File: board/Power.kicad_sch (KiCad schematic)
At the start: 0 parts

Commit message: Added MCU and initial half bridge circuits from application circuit.
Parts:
- added C6: 10µF, Capacitor_SMD:C_1206_3216Metric_Pad1.33x1.80mm_HandSolder, symbol Device:C
- added C7: 10µF, Capacitor_SMD:C_0603_1608Metric_Pad1.08x0.95mm_HandSolder, symbol Device:C
- added Conn1: AndersonPP, symbol MRDT_Connectors:AndersonPP
- added D1, D2, D3: Green, symbol Device:LED
- added R14, R5: 220 Ω, symbol Device:R
- added R4: 1.5 kΩ, symbol Device:R
- added U3: OKI, MRDT_Devices:OKI_Horizontal, symbol MRDT_Devices:OKI
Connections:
- new net: D1.2 (A), R4.2
- new net: D2.2 (A), R5.2
- new net: D3.2 (A), R14.2
- new net +3.3V: R14.1
- new net +5V: C7.1, R5.1, U3.3 (Vo)
- new net GND: C6.2, C7.2, Conn1.1 (GND), D1.1 (K), D2.1 (K), D3.1 (K), U3.2 (GND)
- new net VCC: C6.1, Conn1.4 (PV+), R4.1, U3.1 (Vi)
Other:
- note added: "Power"
- note added: "Power LEDs"

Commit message: Added connections around the MCU from the application circuit from the data sheet, VCC, VDD, VREF+, etc.
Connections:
- net VCC renamed VM
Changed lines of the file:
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@@
 		(on_board yes)
 		(dnp no)
-		(fields_autoplaced yes)
 		(property "Reference" "#PWR019"
 			(at 43.18 30.48 0)
@@
 			)
 		)
-		(property "Value" "VCC"
-			(at 43.18 21.59 0)
-			(effects
-				(font
-					(size 1.27 1.27)
-				)
+		(property "Value" "VM"
+			(at 41.656 22.098 0)
+			(effects
+				(font
+					(size 1.27 1.27)
+				)
+				(justify left)
 			)
 		)
@@
 		(on_board yes)
 		(dnp no)
-		(fields_autoplaced yes)
 		(property "Reference" "#PWR017"
 			(at 31.75 29.21 0)
@@
 			)
 		)
-		(property "Value" "VCC"
-			(at 31.75 20.32 0)
-			(effects
-				(font
-					(size 1.27 1.27)
-				)
+		(property "Value" "VM"
+			(at 30.48 21.59 0)
+			(effects
+				(font
+					(size 1.27 1.27)
+				)
+				(justify left)
 			)
 		)
@@
 		(on_board yes)
 		(dnp no)
-		(fields_autoplaced yes)
 		(property "Reference" "#PWR07"
 			(at 78.74 29.21 0)
@@
 			)
 		)
-		(property "Value" "VCC"
-			(at 78.74 20.32 0)
-			(effects
-				(font
-					(size 1.27 1.27)
-				)
-			)
-		)
+		(property "Value" "VM"
+			(at 77.216 21.59 0)
+			(effects
+				(font
+					(size 1.27 1.27)
+				)
+				(justify left)
+			)
+		)

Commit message: Finished adding component values to circuits, except for 4 filtering capacitors
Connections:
- net +3.3V renamed VDD_2
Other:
- note added: "+3.3 V"
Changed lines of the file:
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@@
+		)
+	)
+	(text "+3.3 V"
+		(exclude_from_sim no)
+		(at 77.978 44.45 0)
+		(effects
+			(font
+				(size 1.27 1.27)
+			)
 		)
 	)
@@
 	(wire
 		(pts
-			(xy 78.74 44.45) (xy 78.74 46.99)
-		)
-		(stroke
-			(width 0)
-			(type default)
-		)
-	)
-	(wire
-		(pts
 			(xy 78.74 38.1) (xy 85.09 38.1)
 		)
@@
 	(wire
 		(pts
-			(xy 78.74 46.99) (xy 85.09 46.99)
+			(xy 82.55 46.99) (xy 85.09 46.99)
 		)
 		(stroke
@@
 			(width 0)
 			(type default)
+		)
+	)
+	(global_label "VDD_2"
+		(shape input)
+		(at 82.55 46.99 180)
+		(fields_autoplaced yes)
+		(effects
+			(font
+				(size 1.27 1.27)
+			)
+			(justify right)
+		)
+		(property "Intersheetrefs" "${INTERSHEET_REFS}"
+			(at 73.7591 46.99 0)
+			(effects
+				(font
+					(size 1.27 1.27)
+				)
+				(justify right)
+				(hide yes)
+			)
 		)
 	)
@@
 					(unit 1)
 				)
-			)
-		)
-	)
-	(symbol
-		(lib_id "power:+3.3V")
-		(at 78.74 44.45 0)
-		(unit 1)
-		(exclude_from_sim no)
-		(in_bom yes)
-		(on_board yes)
-		(dnp no)
-		(property "Reference" "#PWR025"
-			(at 78.74 48.26 0)
-			(effects
-				(font
-					(size 1.27 1.27)
-				)
-				(hide yes)
-			)
-		)
-		(property "Value" "+3.3V"
-			(at 78.74 40.386 0)
-			(effects
-				(font
-					(size 1.27 1.27)
-				)
-			)
-		)
-		(property "Footprint" ""
-			(at 78.74 44.45 0)
-			(effects
-				(font
-					(size 1.27 1.27)
-				)
-				(hide yes)
-			)
-		)
-		(property "Datasheet" ""
-			(at 78.74 44.45 0)
-			(effects
-				(font
-					(size 1.27 1.27)
-				)
-				(hide yes)
-			)
-		)
-		(property "Description" "Power symbol creates a global label with name \"+3.3V\""
-			(at 78.74 44.45 0)
-			(effects
-				(font
-					(size 1.27 1.27)
-				)
-				(hide yes)
-			)
-		)
-		(pin "1"
-		)
-		(instances
-			(project ""
-				(path "/1ef8bc88-f0df-4a97-862b-c4b9ec3b4ed0/b855338b-ea17-4b47-9bba-97d28962f939"
-					(reference "#PWR025")
-					(unit 1)
-				)

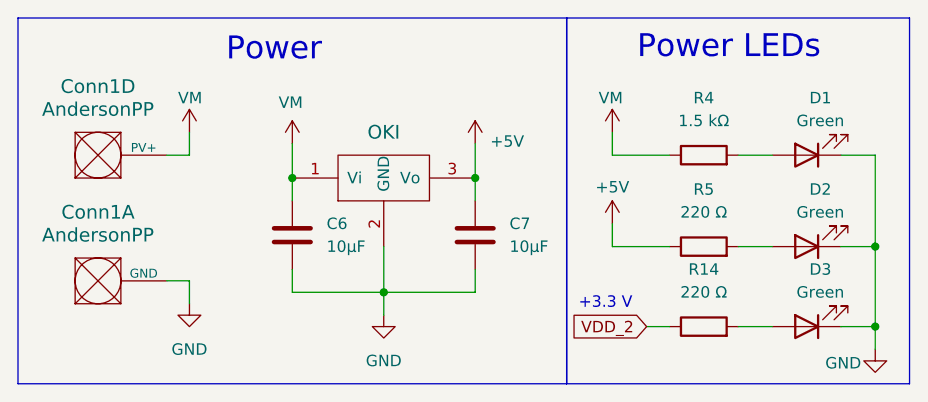
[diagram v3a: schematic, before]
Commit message: Implemented some fixes discussed during the board review.
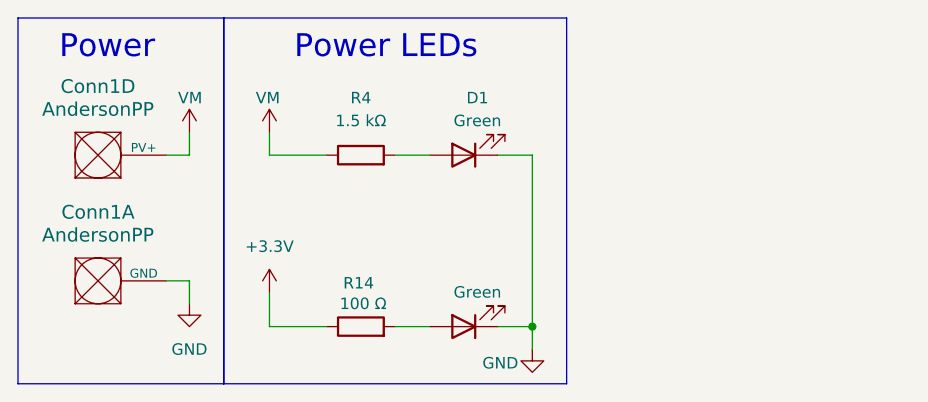
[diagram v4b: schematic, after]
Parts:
- removed C6: 10µF, Capacitor_SMD:C_1206_3216Metric_Pad1.33x1.80mm_HandSolder, symbol Device:C
- removed C7: 10µF, Capacitor_SMD:C_0603_1608Metric_Pad1.08x0.95mm_HandSolder, symbol Device:C
- removed D2: Green, symbol Device:LED
- removed R5: 220 Ω, symbol Device:R
- removed U3: OKI, MRDT_Devices:OKI_Horizontal, symbol MRDT_Devices:OKI
- R14: value 220 Ω -> 100 Ω
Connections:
- net VDD_2 renamed +3.3V
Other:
- note removed: "+3.3 V"
- moved on the sheet: D1, R14, R4

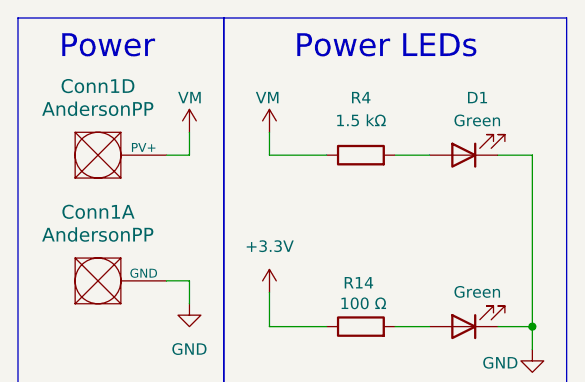
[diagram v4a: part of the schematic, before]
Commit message: Fixed many issues brought up in the schematic review.
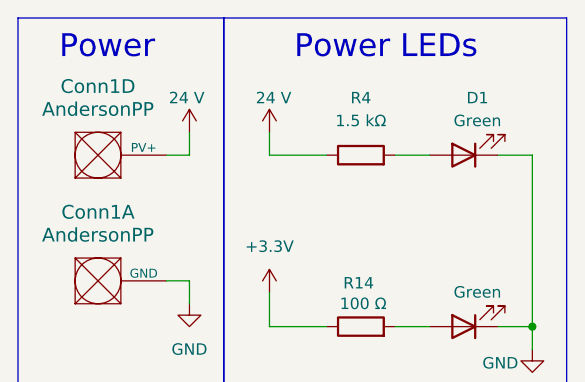
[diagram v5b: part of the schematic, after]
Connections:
- net VM renamed 24 V
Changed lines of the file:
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@@
 			)
 		)
-		(property "Value" "VM"
-			(at 30.48 21.59 0)
+		(property "Value" "24 V"
+			(at 29.464 21.59 0)
 			(effects
 				(font
@@
 			)
 		)
-		(property "Value" "VM"
+		(property "Value" "24 V"
 			(at 39.116 21.59 0)
 			(effects

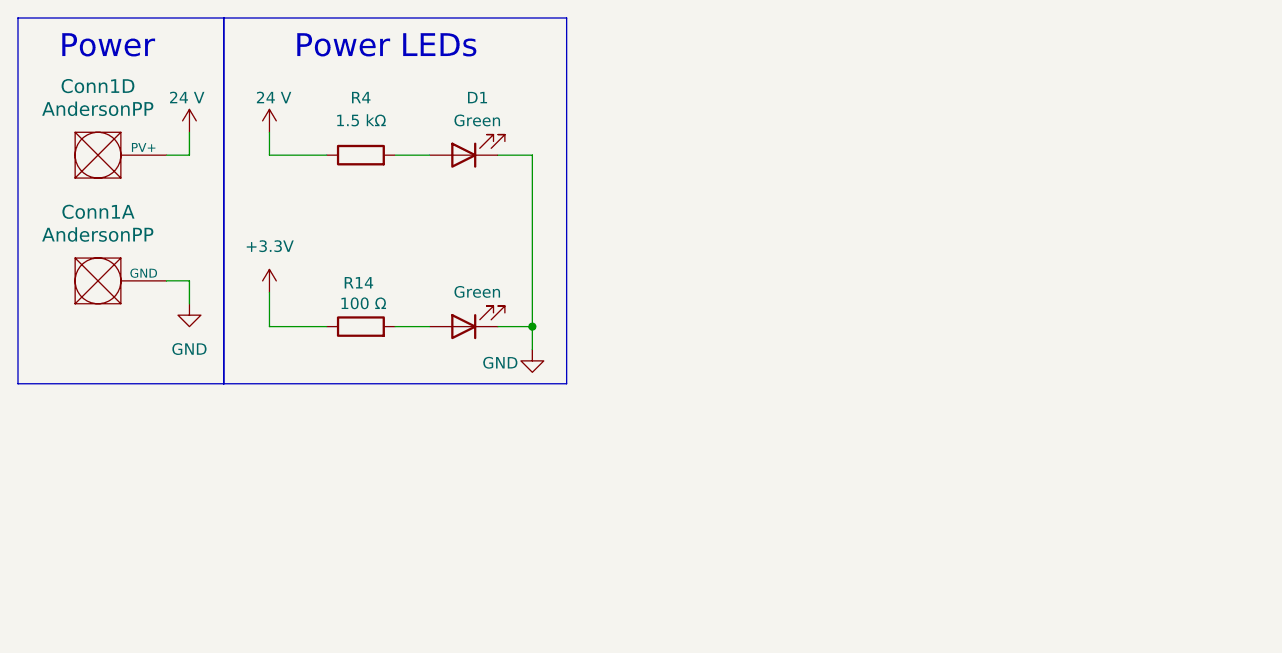
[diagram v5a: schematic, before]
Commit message: Fixed everything mentioned in schematic review, should be ready for second review/layout.
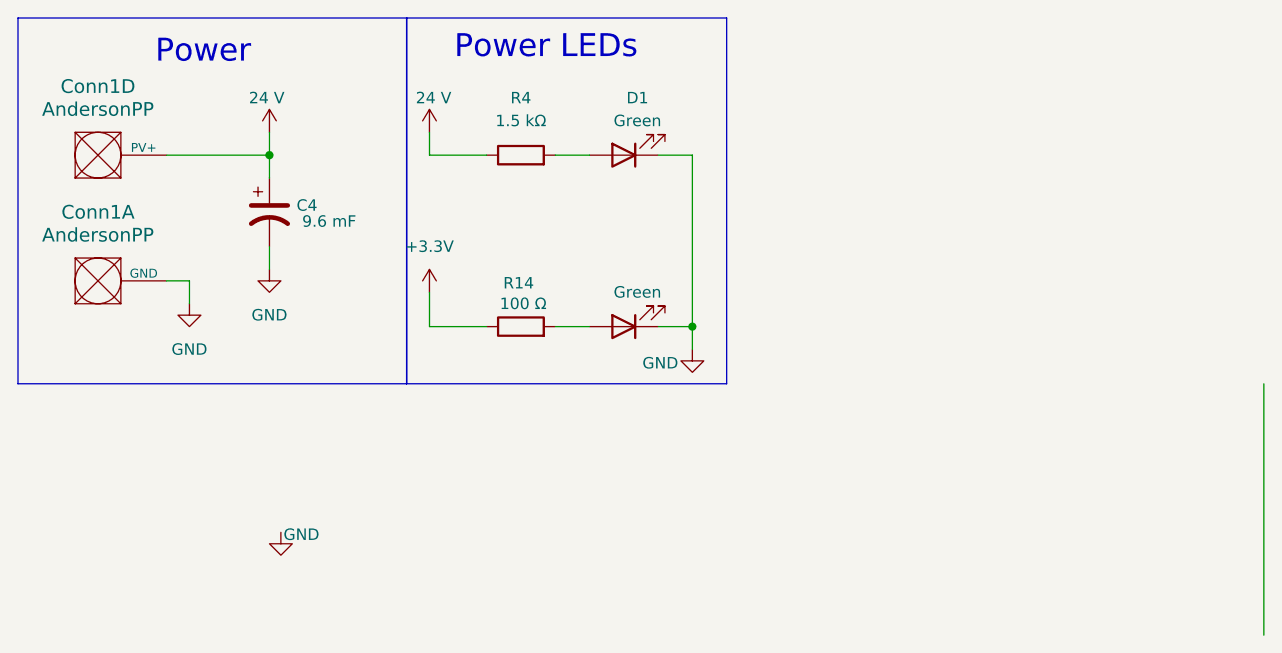
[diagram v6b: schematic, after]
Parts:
- added C4: 9.6 mF, symbol Device:C_Polarized_US
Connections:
- net 24 V: now also C4.1
- net GND: now also C4.2
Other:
- moved on the sheet: D1, R14, R4

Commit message: Updated footprints for schematic
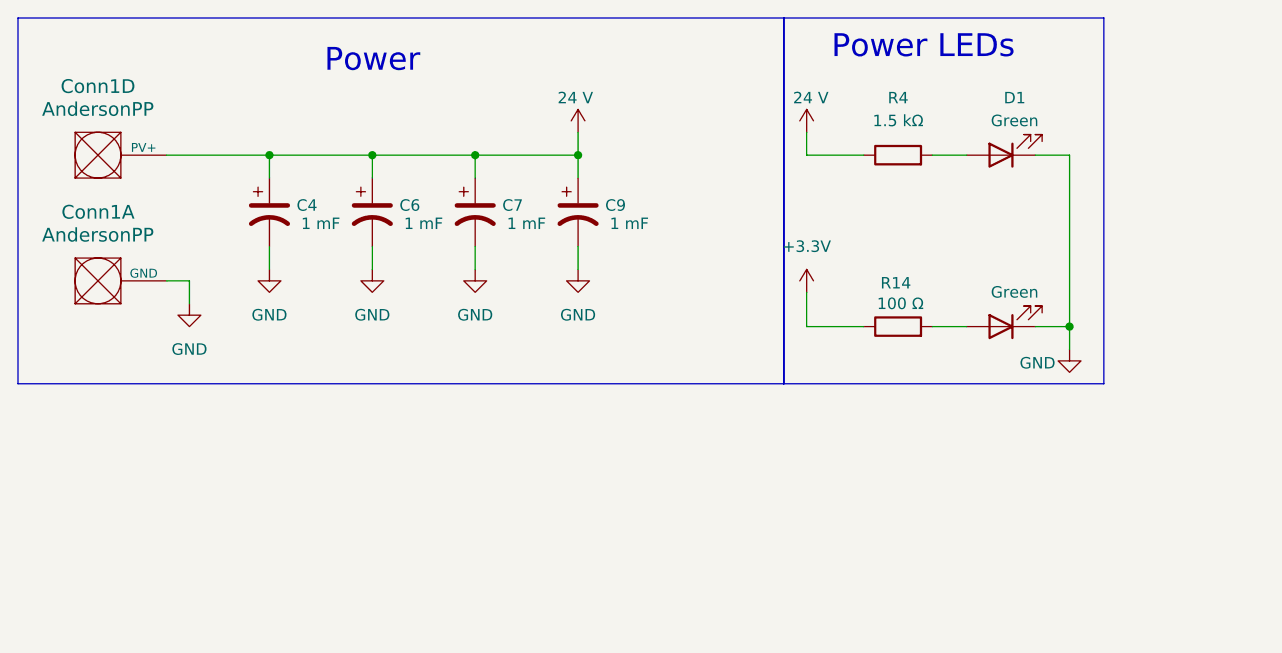
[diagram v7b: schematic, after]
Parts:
- added C6, C7, C9: 1 mF, BoCoFootprintLibrary:U1-Z_NCH, symbol Device:C_Polarized_US
- C4: value 9.6 mF -> 1 mF; footprint (none) -> BoCoFootprintLibrary:U1-Z_NCH
- D1, D3: footprint (none) -> LED_SMD:LED_0603_1608Metric_Pad1.05x0.95mm_HandSolder
- R14, R4: footprint (none) -> Resistor_SMD:R_0603_1608Metric_Pad0.98x0.95mm_HandSolder
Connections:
- net 24 V: now also C6.1, C7.1, C9.1
- net GND: now also C6.2, C7.2, C9.2
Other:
- moved on the sheet: D1, R14, R4

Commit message: Adjusted schematic footprints
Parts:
- Conn1: footprint (none) -> MRDT_Connectors:Square_Anderson_2_H_Side_By_Side_PV
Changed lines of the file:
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@@
 			)
 		)
-		(property "Footprint" ""
+		(property "Footprint" "MRDT_Connectors:Square_Anderson_2_H_Side_By_Side_PV"
 			(at 15.24 44.45 0)
 			(effects
@@
 			)
 		)
-		(property "Footprint" ""
+		(property "Footprint" "MRDT_Connectors:Square_Anderson_2_H_Side_By_Side_PV"
 			(at 15.24 58.42 0)
 			(effects
